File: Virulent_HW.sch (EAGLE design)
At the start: 52 parts, among them U1 STM32F050G6U6

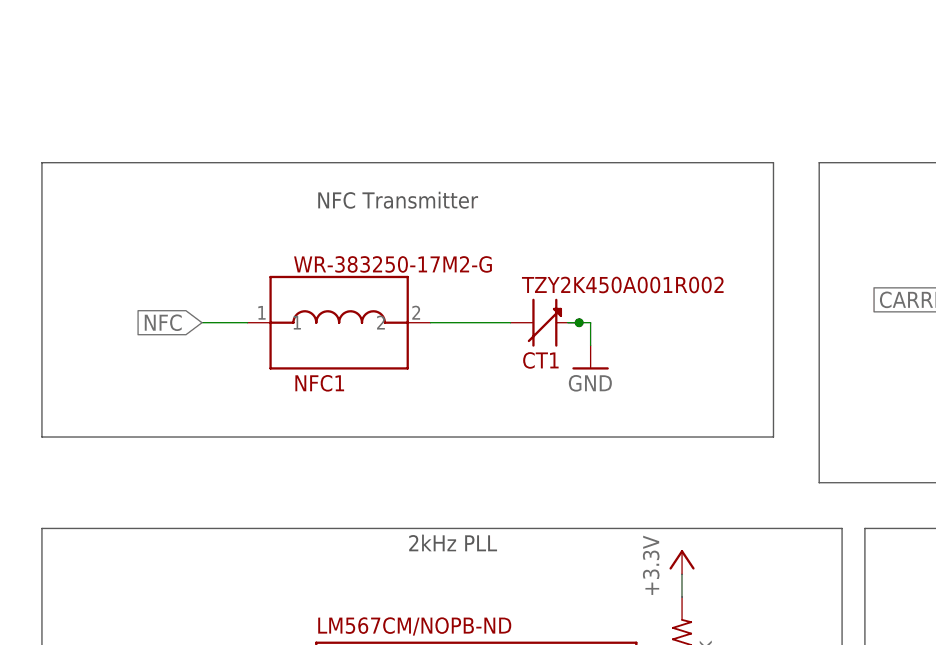
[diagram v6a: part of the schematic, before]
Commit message: added no place capcitor to NFC coil transmitter in case needed
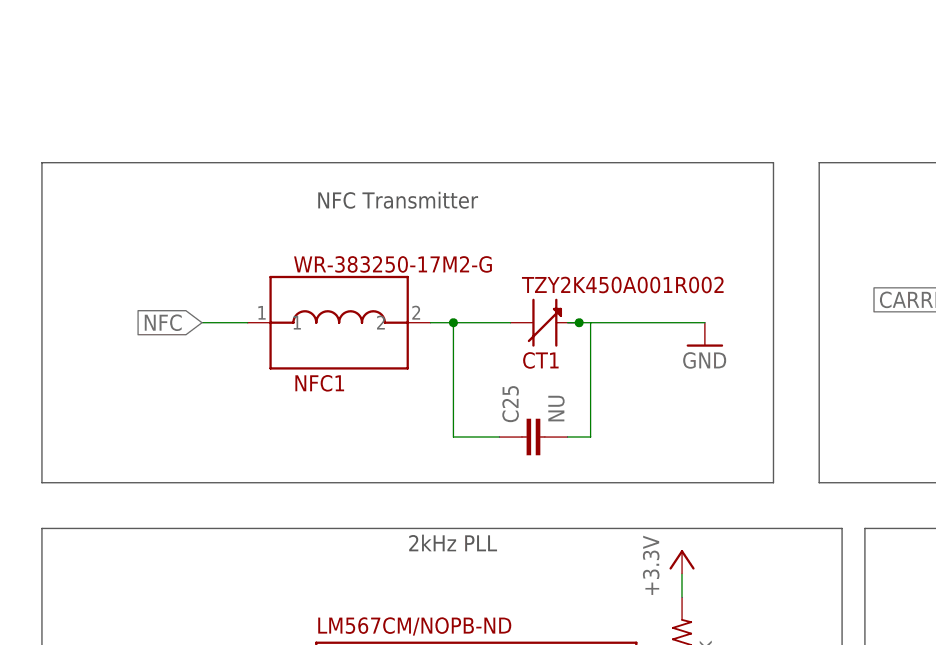
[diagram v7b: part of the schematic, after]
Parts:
- added C25: NU, rcl:C-EUC1206
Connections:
- net GND: now also C25.2
- net N$26: now also C25.1
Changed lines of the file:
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@@
 <part name="GND19" library="Virulent_HW" deviceset="GND" device=""/>
 <part name="NFC1" library="Virulent_HW" deviceset="WR-383250" device="-17M2-G"/>
+<part name="C25" library="rcl" deviceset="C-EU" device="C1206" value="NU"/>
 </parts>
 <sheets>
@@
 <text x="127" y="109.22" size="1.778" layer="97">Frequency Modulation</text>
 <wire x1="10.16" y1="114.3" x2="91.44" y2="114.3" width="0.1524" layer="97"/>
-<wire x1="91.44" y1="114.3" x2="91.44" y2="83.82" width="0.1524" layer="97"/>
-<wire x1="91.44" y1="83.82" x2="10.16" y2="83.82" width="0.1524" layer="97"/>
-<wire x1="10.16" y1="83.82" x2="10.16" y2="114.3" width="0.1524" layer="97"/>
+<wire x1="91.44" y1="114.3" x2="91.44" y2="78.74" width="0.1524" layer="97"/>
+<wire x1="91.44" y1="78.74" x2="10.16" y2="78.74" width="0.1524" layer="97"/>
+<wire x1="10.16" y1="78.74" x2="10.16" y2="114.3" width="0.1524" layer="97"/>
 <text x="40.64" y="109.22" size="1.778" layer="97">NFC Transmitter</text>
 </plain>
@@
 <instance part="GND18" gate="1" x="127" y="83.82"/>
 <instance part="CT1" gate="G$1" x="66.04" y="96.52"/>
-<instance part="GND19" gate="1" x="71.12" y="91.44"/>
+<instance part="GND19" gate="1" x="83.82" y="93.98"/>
 <instance part="NFC1" gate="G$1" x="43.18" y="96.52"/>
+<instance part="C25" gate="G$1" x="63.5" y="83.82" rot="R90"/>
 </instances>
 <busses>
@@
 <wire x1="68.58" y1="96.52" x2="69.85" y2="96.52" width="0.1524" layer="91"/>
 <wire x1="69.85" y1="96.52" x2="71.12" y2="96.52" width="0.1524" layer="91"/>
-<wire x1="71.12" y1="96.52" x2="71.12" y2="93.98" width="0.1524" layer="91"/>
 <pinref part="GND19" gate="1" pin="GND"/>
 <pinref part="CT1" gate="G$1" pin="B@2"/>
 <junction x="69.85" y="96.52"/>
+<wire x1="71.12" y1="96.52" x2="83.82" y2="96.52" width="0.1524" layer="91"/>
+<wire x1="71.12" y1="96.52" x2="71.12" y2="83.82" width="0.1524" layer="91"/>
+<wire x1="71.12" y1="83.82" x2="68.58" y2="83.82" width="0.1524" layer="91"/>
+<pinref part="C25" gate="G$1" pin="2"/>
 </segment>
 </net>
@@
 <pinref part="NFC1" gate="G$1" pin="2@2"/>
 <pinref part="CT1" gate="G$1" pin="A@1"/>
-<wire x1="53.34" y1="96.52" x2="62.23" y2="96.52" width="0.1524" layer="91"/>
-</segment>
-</net>
+<wire x1="53.34" y1="96.52" x2="55.88" y2="96.52" width="0.1524" layer="91"/>
+<wire x1="55.88" y1="96.52" x2="62.23" y2="96.52" width="0.1524" layer="91"/>
+<wire x1="55.88" y1="96.52" x2="55.88" y2="83.82" width="0.1524" layer="91"/>
+<wire x1="55.88" y1="83.82" x2="60.96" y2="83.82" width="0.1524" layer="91"/>
+<pinref part="C25" gate="G$1" pin="1"/>
+<junction x="55.88" y="96.52"/>
+</segment>
+</net>

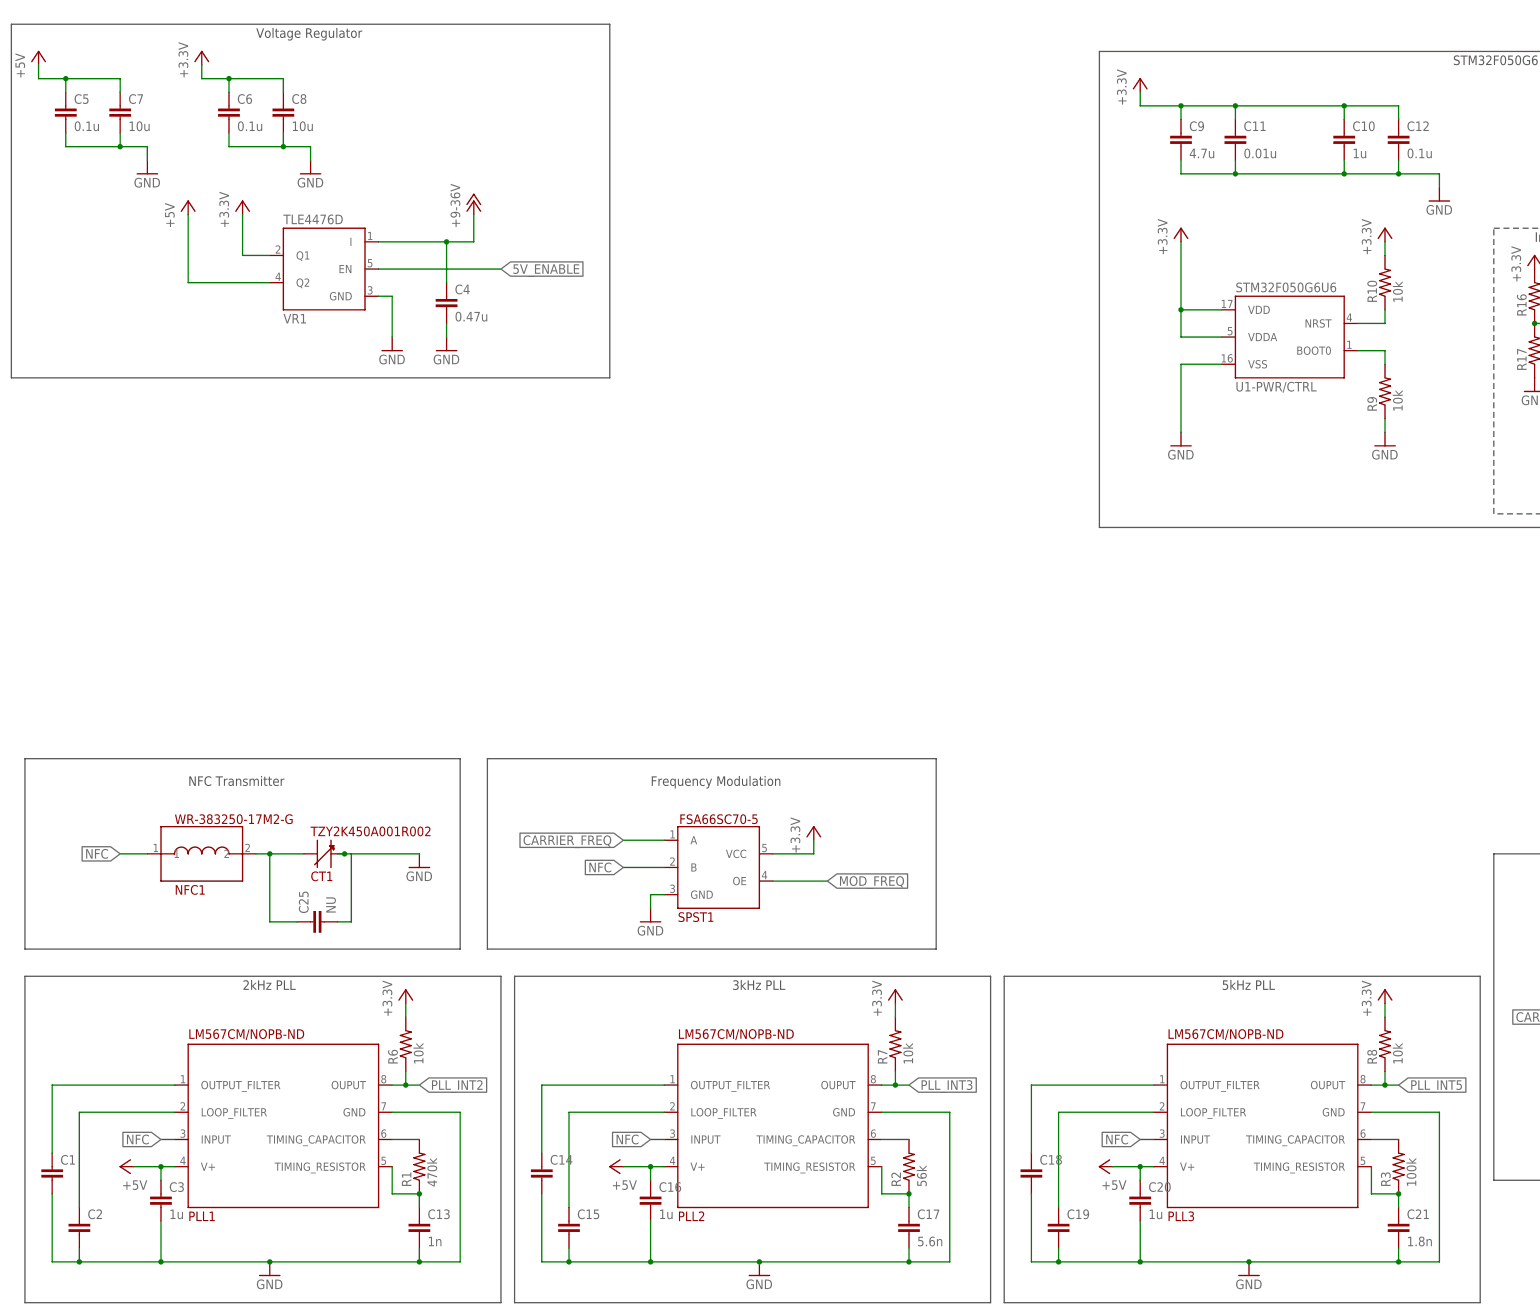
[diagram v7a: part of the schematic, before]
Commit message: updated power symbol and a few revisions suggested by Andrew. Added team information.
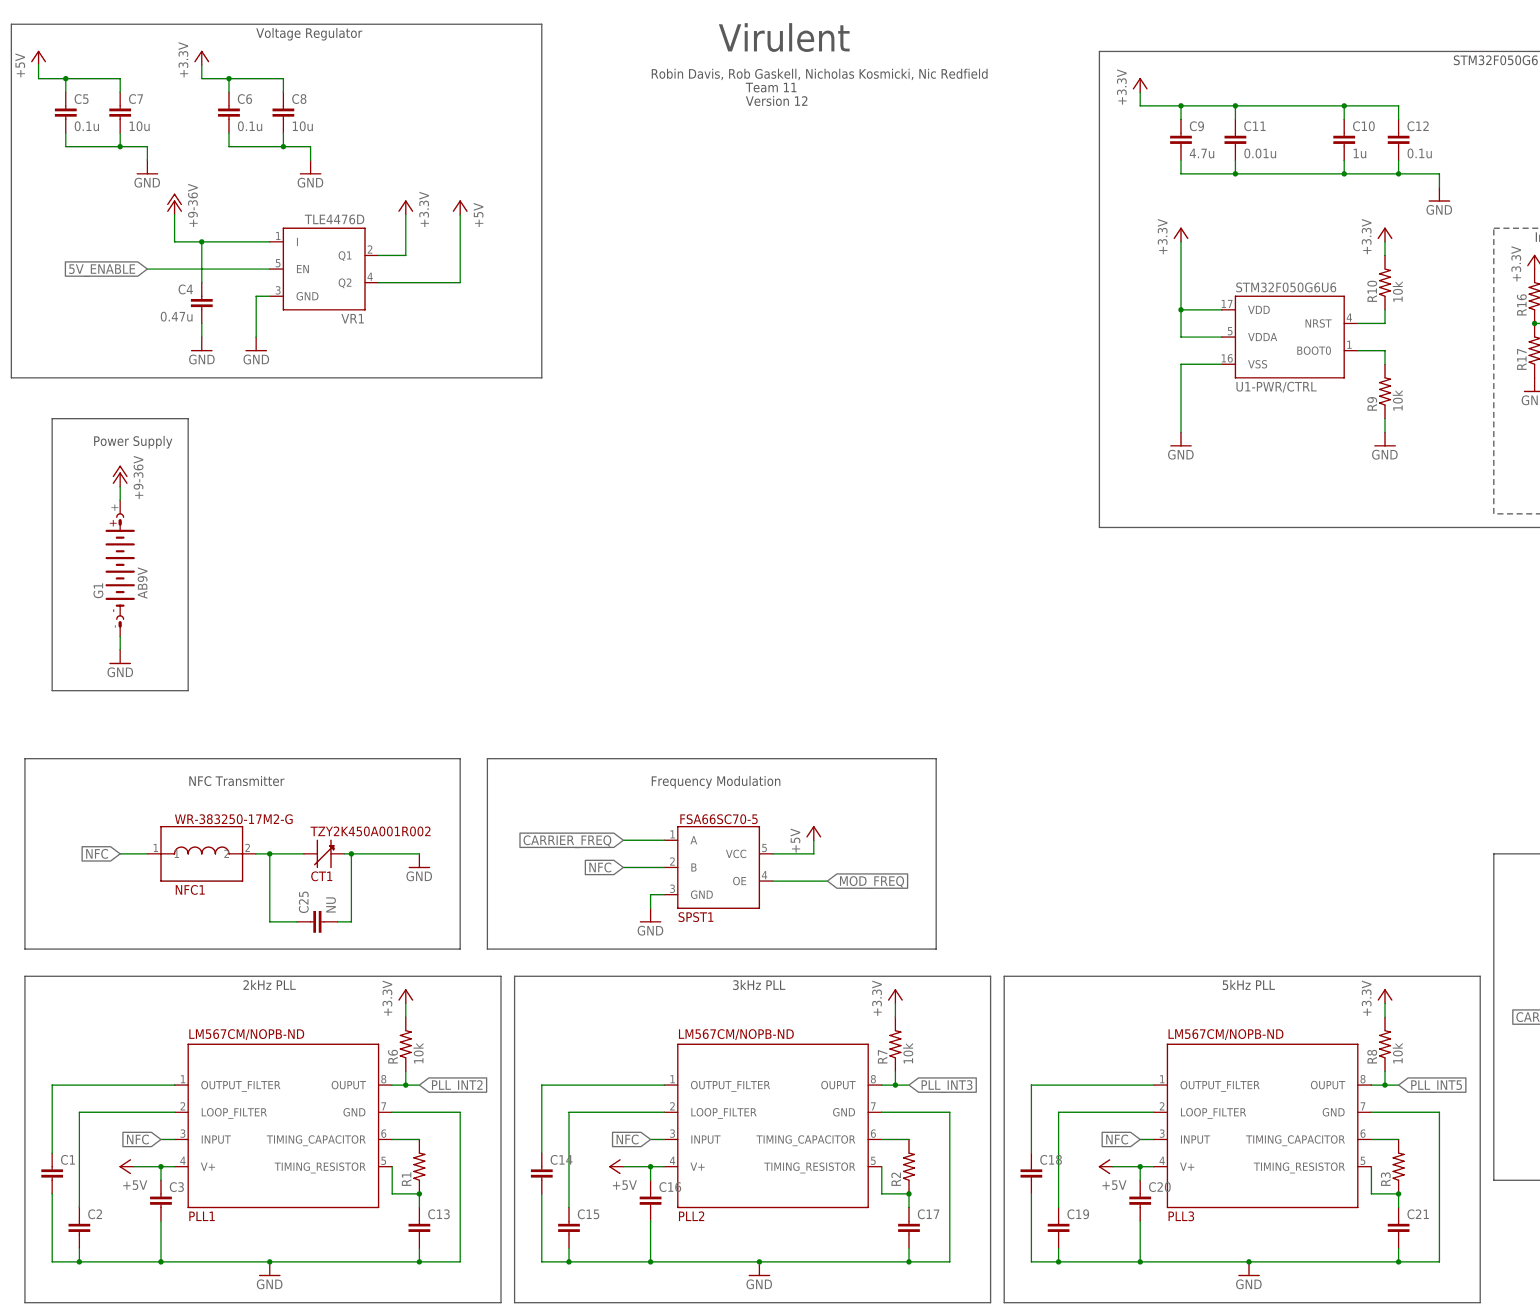
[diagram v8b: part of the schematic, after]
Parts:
- added G1: AB9V, battery:AB9V
- C13: value 1n -> (none)
- C16, C20, C3: value 1u -> (none)
- C17: value 5.6n -> (none)
- C21: value 1.8n -> (none)
- R1: value 470k -> (none)
- R2: value 56k -> (none)
- R3: value 100k -> (none)
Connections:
- net +3.3V: no longer SPST1.VCC@5
- net +5V: now also SPST1.VCC@5
- net +9-36V: now also G1.+
- net GND: now also G1.-
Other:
- note added: "Power Supply"
- note added: "Robin Davis, Rob Gaskell, Nicholas Kosmicki, Nic Redfield"
- note added: "Team 11"
- note added: "Version 12"
- note added: "Virulent"
- moved on the sheet: C4
